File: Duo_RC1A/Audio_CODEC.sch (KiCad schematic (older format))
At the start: 31 parts

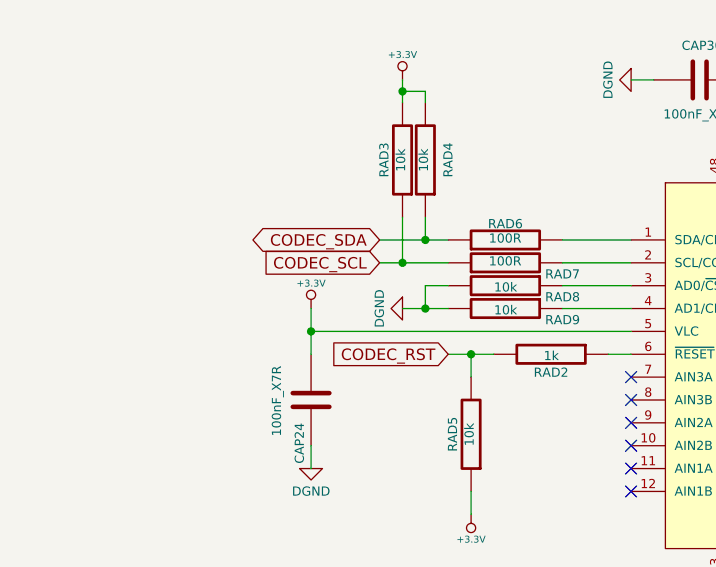
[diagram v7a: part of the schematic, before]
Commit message: Finished all the tracks. Need to place loooots of vias to connect the ground planes of the top and bottom layers.
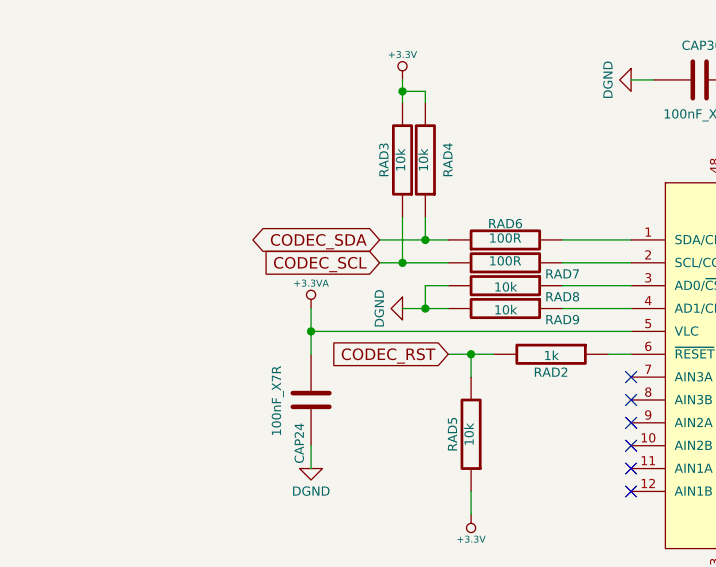
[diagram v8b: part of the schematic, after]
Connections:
- net +3.3V: no longer CAP24.2, UA9.5 (VLC)
- net +3.3VA: now also CAP24.2, UA9.5 (VLC)
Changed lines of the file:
@@
-$EndComp
-$Comp
-L +3.3V #PWR0220
-U 1 1 53D2AFCF
-P 3600 3200
-F 0 "#PWR0220" H 3600 3160 30  0001 C CNN
-F 1 "+3.3V" H 3600 3310 30  0000 C CNN
-F 2 "" H 3600 3200 60  0000 C CNN
-F 3 "" H 3600 3200 60  0000 C CNN
-	1    3600 3200
-	1    0    0    -1
 $EndComp
 $Comp
@@
 	-1   0    0    1
 $EndComp
+$Comp
+L +3.3VA #PWR?
+U 1 1 53D29F9F
+P 3600 3200
+F 0 "#PWR?" H 3600 3160 30  0001 C CNN
+F 1 "+3.3VA" H 3600 3310 30  0000 C CNN
+F 2 "" H 3600 3200 60  0000 C CNN
+F 3 "" H 3600 3200 60  0000 C CNN
+	1    3600 3200
+	1    0    0    -1
+$EndComp
 $EndSCHEMATC
